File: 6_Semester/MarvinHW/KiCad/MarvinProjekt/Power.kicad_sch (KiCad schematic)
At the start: 0 parts

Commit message: added datasheets and worked on schematic
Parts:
- added C37, C38: C, symbol Device:C
- added U8: TPLP5907MFX-3.3, symbol Library:TPLP5907MFX-3.3
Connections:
- new net +3.3V: C38.1, U8.5 (VOUT)
- new net GND: C37.2, C38.2, U8.2 (GND)
- new net V_BAT: C37.1, U8.1 (VIN)
- no-connect marks 0 -> 1

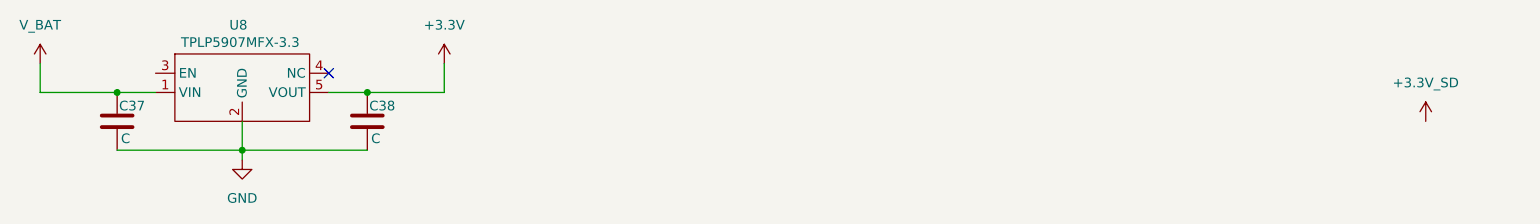
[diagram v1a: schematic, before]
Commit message: renamed untitledsheet to crontrol
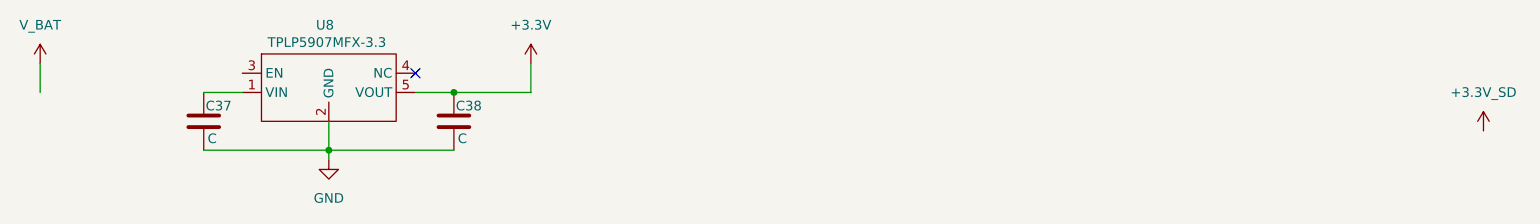
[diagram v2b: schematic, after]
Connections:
- net V_BAT: no longer C37.1, U8.1 (VIN)
- new net: C37.1, U8.1 (VIN)
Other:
- moved on the sheet: C37, C38, U8
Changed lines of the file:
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@@
 	(paper "A4")
 	(junction
-		(at 68.58 33.02)
+		(at 80.01 33.02)
 		(diameter 0)
 		(color 0 0 0 0)
 	)
 	(junction
-		(at 52.07 40.64)
+		(at 63.5 40.64)
 		(diameter 0)
 		(color 0 0 0 0)
 	)
-	(junction
-		(at 35.56 33.02)
-		(diameter 0)
-		(color 0 0 0 0)
-	)
 	(no_connect
-		(at 63.5 30.48)
-	)
-	(wire
-		(pts
-			(xy 78.74 29.21) (xy 78.74 33.02)
-		)
-		(stroke
-			(width 0)
-			(type default)
-		)
-	)
-	(wire
-		(pts
-			(xy 35.56 33.02) (xy 40.64 33.02)
-		)
-		(stroke
-			(width 0)
-			(type default)
-		)
-	)
-	(wire
-		(pts
-			(xy 78.74 33.02) (xy 68.58 33.02)
-		)
-		(stroke
-			(width 0)
-			(type default)
-		)
-	)
-	(wire
-		(pts
-			(xy 63.5 33.02) (xy 68.58 33.02)
-		)
-		(stroke
-			(width 0)
-			(type default)
-		)
-	)
-	(wire
-		(pts
-			(xy 52.07 36.83) (xy 52.07 40.64)
-		)
-		(stroke
-			(width 0)
-			(type default)
-		)
-	)
-	(wire
-		(pts
-			(xy 25.4 33.02) (xy 35.56 33.02)
-		)
-		(stroke
-			(width 0)
-			(type default)
-		)
-	)
-	(wire
-		(pts
-			(xy 52.07 40.64) (xy 68.58 40.64)
-		)
-		(stroke
-			(width 0)
-			(type default)
-		)
-	)
-	(wire
-		(pts
-			(xy 52.07 41.91) (xy 52.07 40.64)
-		)
-		(stroke
-			(width 0)
-			(type default)
-		)
-	)
-	(wire
-		(pts
-			(xy 35.56 40.64) (xy 52.07 40.64)
+		(at 74.93 30.48)
+	)
+	(wire
+		(pts
+			(xy 90.17 29.21) (xy 90.17 33.02)
+		)
+		(stroke
+			(width 0)
+			(type default)
+		)
+	)
+	(wire
+		(pts
+			(xy 46.99 33.02) (xy 52.07 33.02)
+		)
+		(stroke
+			(width 0)
+			(type default)
+		)
+	)
+	(wire
+		(pts
+			(xy 90.17 33.02) (xy 80.01 33.02)
+		)
+		(stroke
+			(width 0)
+			(type default)
+		)
+	)
+	(wire
+		(pts
+			(xy 74.93 33.02) (xy 80.01 33.02)
+		)
+		(stroke
+			(width 0)
+			(type default)
+		)
+	)
+	(wire
+		(pts
+			(xy 63.5 36.83) (xy 63.5 40.64)
+		)
+		(stroke
+			(width 0)
+			(type default)
+		)
+	)
+	(wire
+		(pts
+			(xy 63.5 40.64) (xy 80.01 40.64)
+		)
+		(stroke
+			(width 0)
+			(type default)
+		)
+	)
+	(wire
+		(pts
+			(xy 63.5 41.91) (xy 63.5 40.64)
+		)
+		(stroke
+			(width 0)
+			(type default)
+		)
+	)
+	(wire
+		(pts
+			(xy 46.99 40.64) (xy 63.5 40.64)
 		)
 		(stroke
@@
 	(symbol
 		(lib_id "Library:TPLP5907MFX-3.3")
-		(at 52.07 34.29 0)
+		(at 63.5 34.29 0)
 		(unit 1)
 		(exclude_from_sim no)
@@
 		(dnp no)
 		(property "Reference" "U8"
-			(at 51.562 24.13 0)
+			(at 62.992 24.13 0)
 			(effects
 				(font
@@
 		)
 		(property "Value" "TPLP5907MFX-3.3"
-			(at 51.816 26.416 0)
-			(effects
-				(font
-					(size 1.27 1.27)
-				)
-			)
-		)
-		(property "Footprint" ""
-			(at 52.07 34.29 0)
+			(at 63.246 26.416 0)
+			(effects
+				(font
+					(size 1.27 1.27)
+				)
+			)
+		)
+		(property "Footprint" ""
+			(at 63.5 34.29 0)
 			(effects
 				(font
@@
 		)
 		(property "Datasheet" ""
-			(at 52.07 34.29 0)
+			(at 63.5 34.29 0)
 			(effects
 				(font
@@
 		)
 		(property "Description" ""
-			(at 52.07 34.29 0)
+			(at 63.5 34.29 0)
 			(effects
 				(font
@@
 	(symbol
 		(lib_id "Device:C")
-		(at 35.56 36.83 0)
+		(at 46.99 36.83 0)
 		(unit 1)
 		(exclude_from_sim no)
@@
 		(dnp no)
 		(property "Reference" "C37"
-			(at 35.814 34.798 0)
+			(at 47.244 34.798 0)
 			(effects
 				(font
@@
 		)
 		(property "Value" "C"
-			(at 36.068 39.116 0)
+			(at 47.498 39.116 0)
 			(effects
 				(font
@@
 		)
 		(property "Footprint" ""
-			(at 36.5252 40.64 0)
+			(at 47.9552 40.64 0)
 			(effects
 				(font
@@
 		)
 		(property "Datasheet" "~"
-			(at 35.56 36.83 0)
+			(at 46.99 36.83 0)
 			(effects
 				(font
@@
 		)
 		(property "Description" "Unpolarized capacitor"
-			(at 35.56 36.83 0)
+			(at 46.99 36.83 0)
 			(effects
 				(font
@@
 	(symbol
 		(lib_id "power:+3.3V")
-		(at 78.74 29.21 0)
+		(at 90.17 29.21 0)
 		(unit 1)
 		(exclude_from_sim no)
@@
 		(fields_autoplaced yes)
 		(property "Reference" "#PWR065"
-			(at 78.74 33.02 0)
+			(at 90.17 33.02 0)
 			(effects
 				(font
@@
 		)
 		(property "Value" "+3.3V"
-			(at 78.74 24.13 0)
-			(effects
-				(font
-					(size 1.27 1.27)
-				)
-			)
-		)
-		(property "Footprint" ""
-			(at 78.74 29.21 0)
+			(at 90.17 24.13 0)
+			(effects
+				(font
+					(size 1.27 1.27)
+				)
+			)
+		)
+		(property "Footprint" ""
+			(at 90.17 29.21 0)
 			(effects
 				(font
@@
 		)
 		(property "Datasheet" ""
-			(at 78.74 29.21 0)
+			(at 90.17 29.21 0)
 			(effects
 				(font
@@
 		)
 		(property "Description" "Power symbol creates a global label with name \"+3.3V\""
-			(at 78.74 29.21 0)
+			(at 90.17 29.21 0)
 			(effects
 				(font
@@
 	(symbol
 		(lib_id "power:+3.3V")
-		(at 208.28 36.83 0)
+		(at 215.9 38.1 0)
 		(unit 1)
 		(exclude_from_sim no)
@@
 		(fields_autoplaced yes)
 		(property "Reference" "#PWR062"
-			(at 208.28 40.64 0)
+			(at 215.9 41.91 0)
 			(effects
 				(font
@@
 		)
 		(property "Value" "+3.3V_SD"
-			(at 208.28 31.75 0)
-			(effects
-				(font
-					(size 1.27 1.27)
-				)
-			)
-		)
-		(property "Footprint" ""
-			(at 208.28 36.83 0)
+			(at 215.9 33.02 0)
+			(effects
+				(font
+					(size 1.27 1.27)
+				)
+			)
+		)
+		(property "Footprint" ""
+			(at 215.9 38.1 0)
 			(effects
 				(font
@@
 		)
 		(property "Datasheet" ""
-			(at 208.28 36.83 0)
+			(at 215.9 38.1 0)
 			(effects
 				(font
@@
 		)
 		(property "Description" "Power symbol creates a global label with name \"+3.3V\""
-			(at 208.28 36.83 0)
+			(at 215.9 38.1 0)
 			(effects
 				(font
@@
 	(symbol
 		(lib_id "power:GND")
-		(at 52.07 41.91 0)
+		(at 63.5 41.91 0)
 		(unit 1)
 		(exclude_from_sim no)
@@
 		(fields_autoplaced yes)
 		(property "Reference" "#PWR063"
-			(at 52.07 48.26 0)
+			(at 63.5 48.26 0)
 			(effects
 				(font
@@
 		)
 		(property "Value" "GND"
-			(at 52.07 46.99 0)
-			(effects
-				(font
-					(size 1.27 1.27)
-				)
-			)
-		)
-		(property "Footprint" ""
-			(at 52.07 41.91 0)
+			(at 63.5 46.99 0)
+			(effects
+				(font
+					(size 1.27 1.27)
+				)
+			)
+		)
+		(property "Footprint" ""
+			(at 63.5 41.91 0)
 			(effects
 				(font
@@
 		)
 		(property "Datasheet" ""
-			(at 52.07 41.91 0)
+			(at 63.5 41.91 0)
 			(effects
 				(font
@@
 		)
 		(property "Description" "Power symbol creates a global label with name \"GND\" , ground"
-			(at 52.07 41.91 0)
+			(at 63.5 41.91 0)
 			(effects
 				(font
@@
 	(symbol
 		(lib_id "Device:C")
-		(at 68.58 36.83 0)
+		(at 80.01 36.83 0)
 		(unit 1)
 		(exclude_from_sim no)
@@
 		(dnp no)
 		(property "Reference" "C38"
-			(at 68.834 34.798 0)
+			(at 80.264 34.798 0)
 			(effects
 				(font
@@
 		)
 		(property "Value" "C"
-			(at 69.088 39.116 0)
+			(at 80.518 39.116 0)
 			(effects
 				(font
@@
 		)
 		(property "Footprint" ""
-			(at 69.5452 40.64 0)
+			(at 80.9752 40.64 0)
 			(effects
 				(font
@@
 		)
 		(property "Datasheet" "~"
-			(at 68.58 36.83 0)
+			(at 80.01 36.83 0)
 			(effects
 				(font
@@
 		)
 		(property "Description" "Unpolarized capacitor"
-			(at 68.58 36.83 0)
-			(effects
-				(font
+			(at 80.01 36.83 0)
+			(effects
+				(font

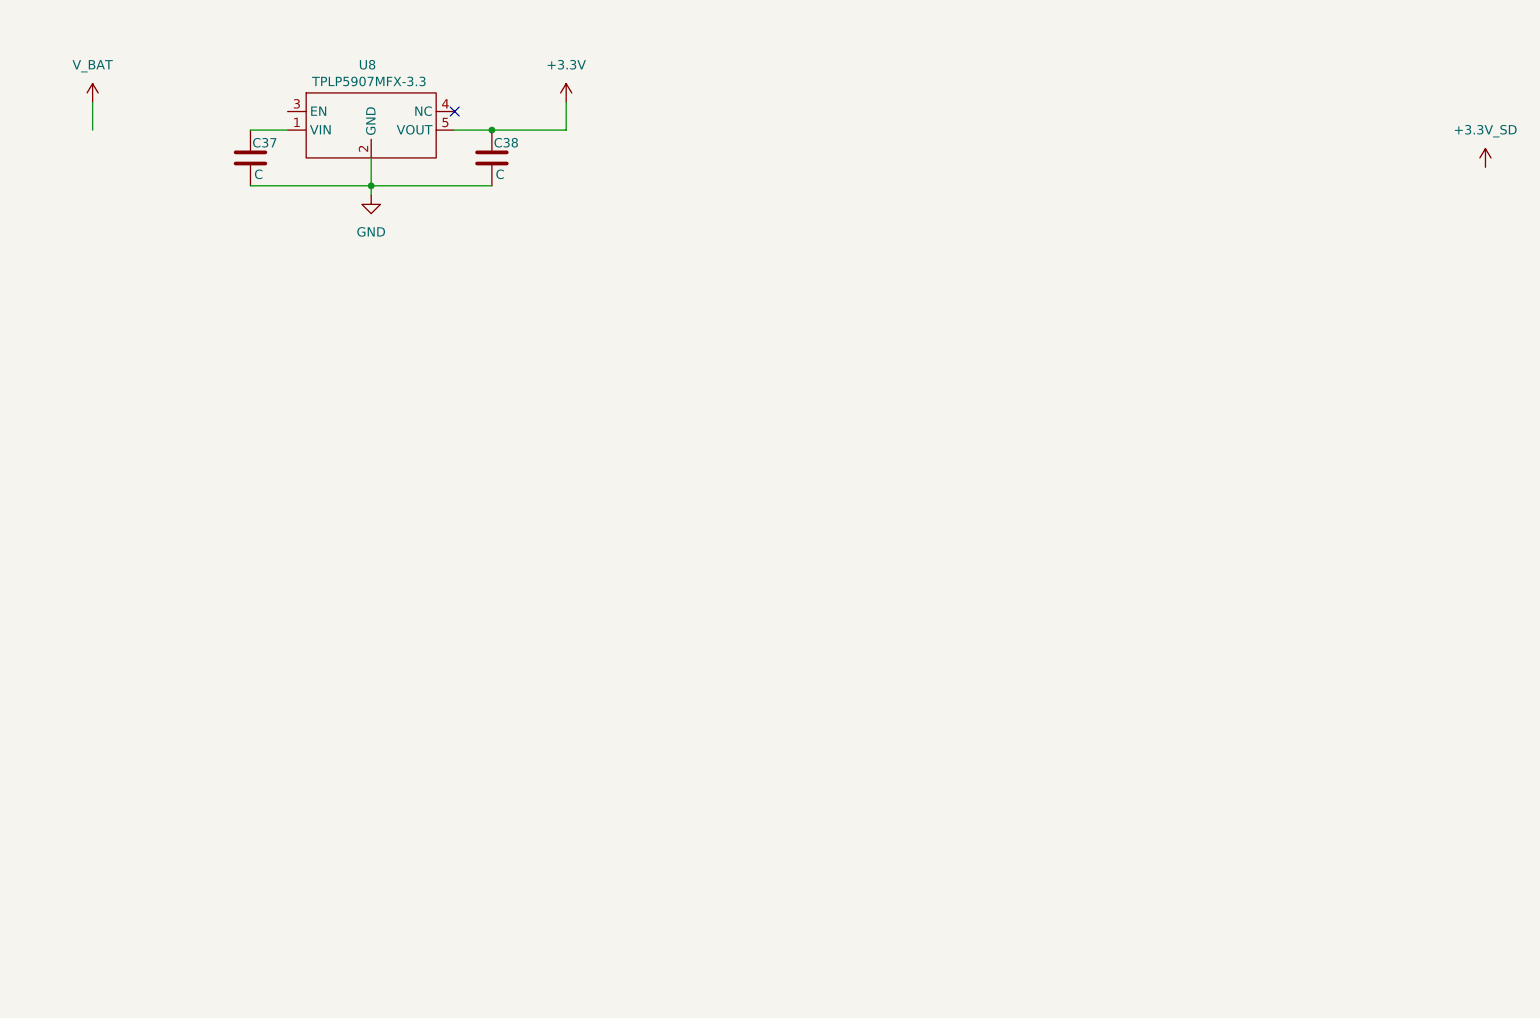
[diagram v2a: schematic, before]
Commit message: finished schematic working on footprints
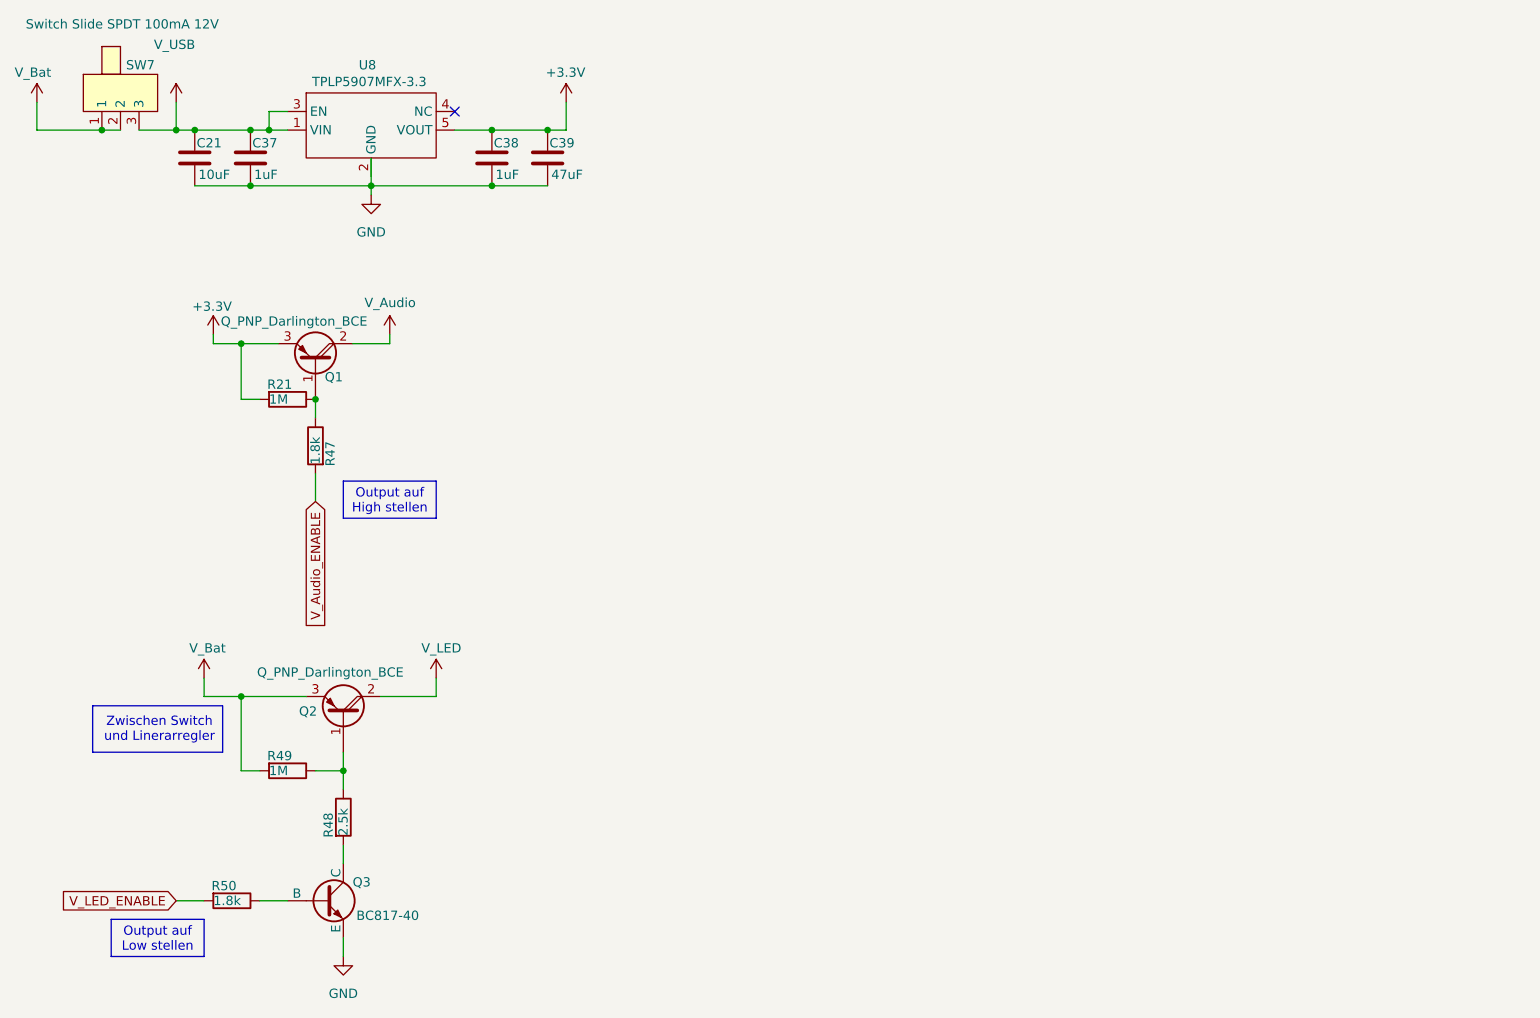
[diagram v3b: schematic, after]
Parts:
- added C21: 10uF, Capacitor_SMD:C_1206_3216Metric_Pad1.33x1.80mm_HandSolder, symbol Device:C
- added C39: 47uF, Capacitor_SMD:CP_Elec_6.3x5.9, symbol Device:C
- added Q1, Q2: Q_PNP_Darlington_BCE, symbol Device:Q_PNP_Darlington_BCE
- added Q3: BC817-40, Package_TO_SOT_SMD:SOT-23, symbol Simulation_SPICE:NPN
- added R21, R49: 1M, Resistor_SMD:R_0805_2012Metric_Pad1.20x1.40mm_HandSolder, symbol Device:R
- added R47, R50: 1.8k, Resistor_SMD:R_0805_2012Metric_Pad1.20x1.40mm_HandSolder, symbol Device:R
- added R48: 2.5k, Resistor_SMD:R_0805_2012Metric_Pad1.20x1.40mm_HandSolder, symbol Device:R
- added SW7: Switch Slide SPDT 100mA 12V, Matrix2_Schnuppiprojekt:SW-OS102011MA10QN1, symbol Eduboard_Kicadlib:1FS1T1B9M2RES-5
- C37, C38: value C -> 1uF; footprint (none) -> Capacitor_SMD:C_0805_2012Metric_Pad1.18x1.45mm_HandSolder
- U8: footprint (none) -> Package_TO_SOT_SMD:SOT-23-5_HandSoldering
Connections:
- net +3.3V: now also C39.1, Q1.3 (E), R21.2
- net GND: now also C21.2, C39.2, Q3.3 (E); no longer U8.2 (GND)
- net V_USB: now reaches C37.1, U8.1 (VIN)
- net V_USB: now also U8.3 (EN), C21.1, SW7.3
- new net: Q3.1 (C), R48.2
- new net: Q3.2 (B), R50.1
- new net: Q1.1 (B), R21.1, R47.1
- new net: Q2.1 (B), R48.1, R49.1
- new net V_Audio: Q1.2 (C)
- new net V_Audio_ENABLE: R47.2
- new net V_Bat: Q2.3 (E), R49.2, SW7.1, SW7.2
- new net V_LED: Q2.2 (C)
- new net V_LED_ENABLE: R50.2
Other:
- note added: "Output auf High stellen"
- note added: "Output auf Low stellen"
- note added: "Zwischen Switch und Linerarregler"
- moved on the sheet: U8

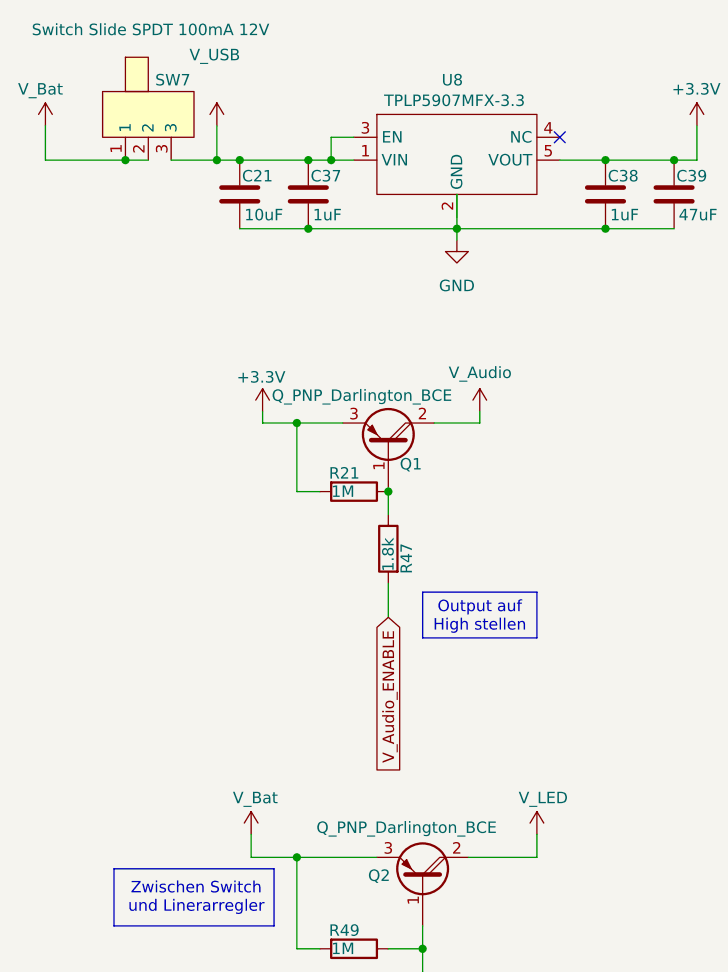
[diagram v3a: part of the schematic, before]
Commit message: finished all footprints and put the objects in place
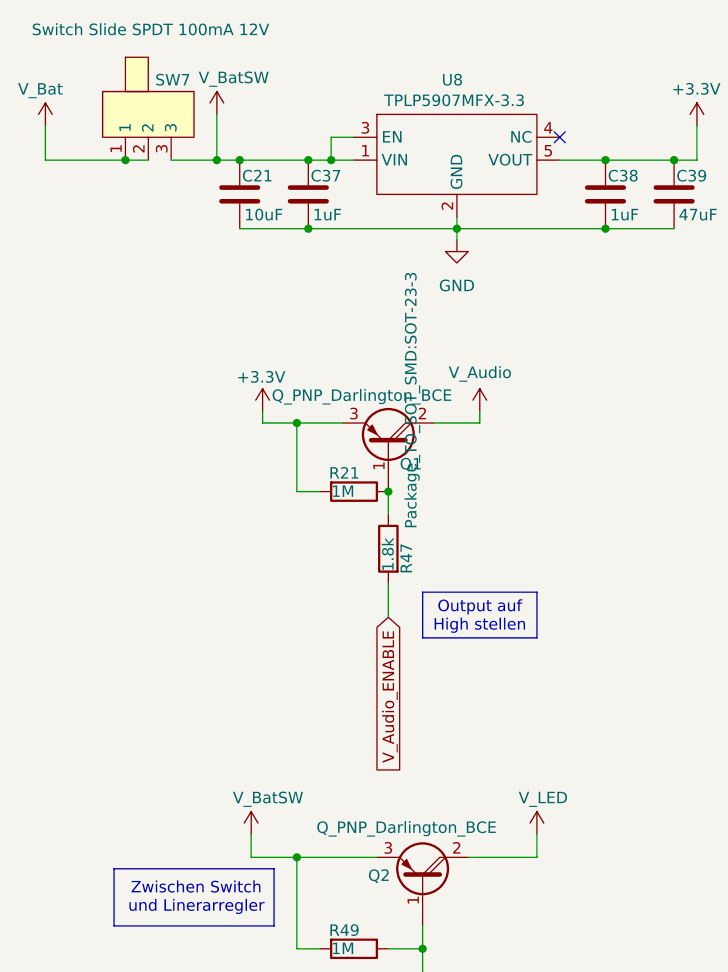
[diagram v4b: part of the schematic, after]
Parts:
- Q1, Q2: footprint (none) -> Package_TO_SOT_SMD:SOT-23-3
- SW7: footprint Matrix2_Schnuppiprojekt:SW-OS102011MA10QN1 -> Library:SW
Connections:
- net GND: now also U8.2 (GND)
- net V_Bat: no longer Q2.3 (E), R49.2
- net V_USB renamed V_BatSW
- net V_BatSW: now also Q2.3 (E), R49.2
